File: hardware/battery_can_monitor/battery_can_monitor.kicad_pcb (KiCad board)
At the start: 2 copper layers, 70 x 90 mm, 71 parts, among them J1 sense3, J10 int, J11 GPIO, J12 GPIO, J13 power, J14 CAN_PWR, J15 CANGND, J2 sense1, J3 Conn_01x05_Male, J4 RJ45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

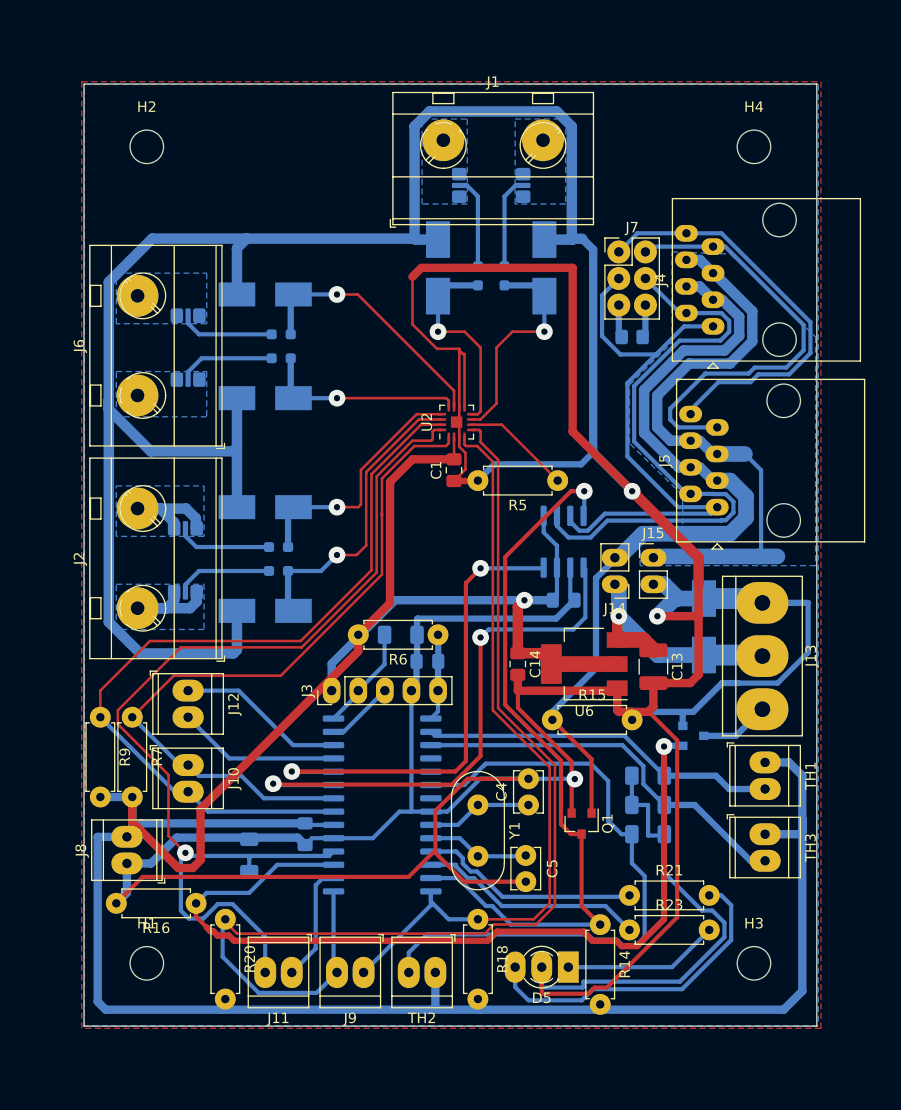
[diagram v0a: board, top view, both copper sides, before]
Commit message: Add a 6mm margin around PCB.
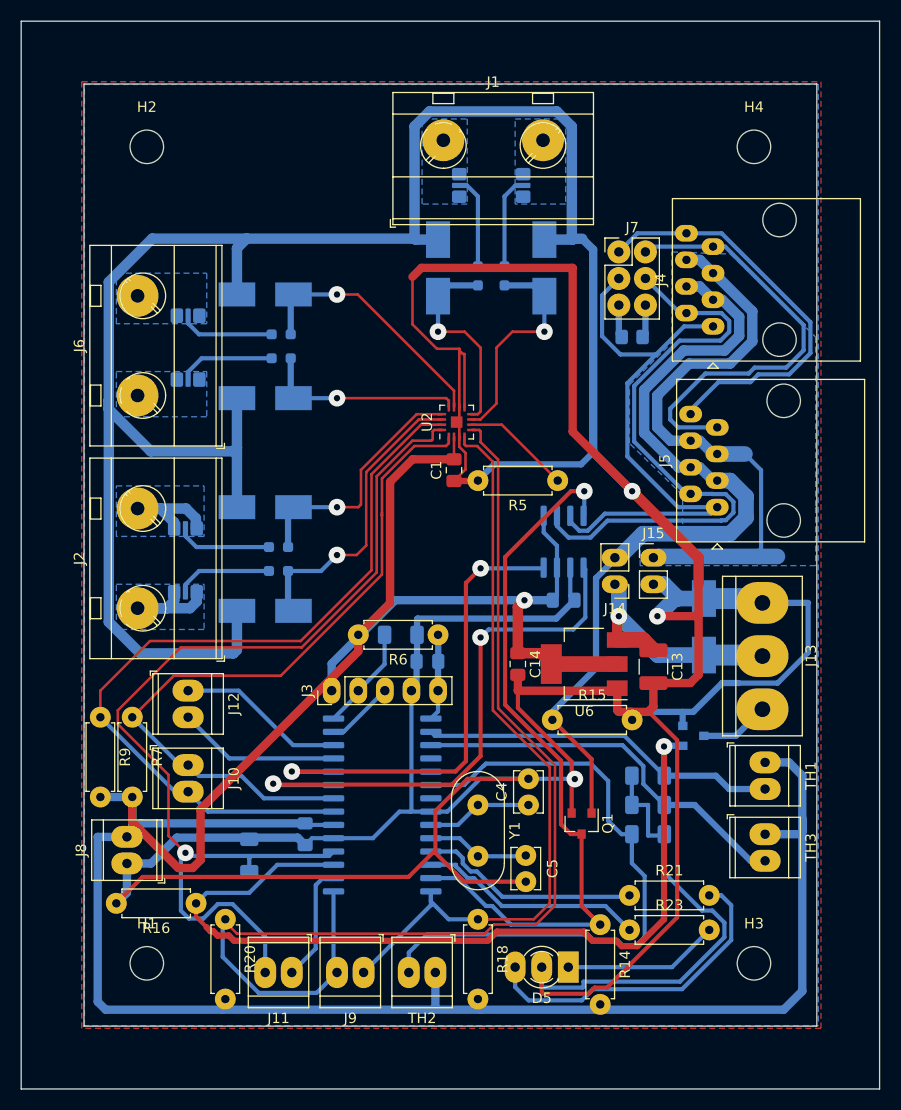
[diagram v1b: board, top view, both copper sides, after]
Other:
- board size 70 x 90 mm -> 82 x 102 mm
